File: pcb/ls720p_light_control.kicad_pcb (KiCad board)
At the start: 2 copper layers, 40 x 20 mm, 20 parts, among them J1 PWR, J2 AVRISP MK2, J3 LED_CONN, Q1 G35N02K, U1 ATTINY5, U2 SLHT50H

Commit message: added ALT parts for LDO, MOSFET, MCU
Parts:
- added SW1: PWR_SWITCH, Connector_PinHeader_2.54mm:PinHeader_1x02_P2.54mm_Vertical, F.Cu at (210.0, 106.7)
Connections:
- J1 pad 2: +12V -> Net-(J1-Pin_2)
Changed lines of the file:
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@@
 			(layers "*.Cu" "*.Mask")
 			(remove_unused_layers no)
-			(net "+12V")
+			(net "Net-(J1-Pin_2)")
 			(pinfunction "Pin_2_2")
 			(pintype "passive")
@@
 			(pintype "passive")
 		)
+		(embedded_fonts no)
+		(model "${KICAD10_3DMODEL_DIR}/Connector_PinHeader_2.54mm.3dshapes/PinHeader_1x02_P2.54mm_Vertical.step"
+			(offset
+				(xyz 0 0 0)
+			)
+			(scale
+				(xyz 1 1 1)
+			)
+			(rotate
+				(xyz 0 0 0)
+			)
+		)
+	)
+	(footprint "Connector_PinHeader_2.54mm:PinHeader_1x02_P2.54mm_Vertical"
+		(layer "F.Cu")
+		(at 209.975 106.7 -90)
+		(descr "Through hole straight pin header, 1x02, 2.54mm pitch, single row")
+		(tags "Through hole pin header THT 1x02 2.54mm single row")
+		(property "Reference" "SW1"
+			(at 0 -2.725 270)
+			(layer "F.SilkS")
+			(effects
+				(font
+					(size 1 1)
+					(thickness 0.15)
+				)
+			)
+		)
+		(property "Value" "PWR_SWITCH"
+			(at 0 4.919999 90)
+			(layer "F.Fab")
+			(effects
+				(font
+					(size 1 1)
+					(thickness 0.15)
+				)
+			)
+		)
+		(property "Datasheet" ""
+			(at 0 0 90)
+			(layer "F.Fab")
+			(hide yes)
+			(effects
+				(font
+					(size 1.27 1.27)
+				)
+			)
+		)
+		(property "Description" "Single Pole Single Throw (SPST) switch"
+			(at 0 0 90)
+			(layer "F.Fab")
+			(hide yes)
+			(effects
+				(font
+					(size 1.27 1.27)
+				)
+			)
+		)
+		(property "KiLib_Generator" "connector/pin_header_socket"
+			(at 0 0 90)
+			(layer "F.SilkS")
+			(hide yes)
+			(effects
+				(font
+					(size 1 1)
+					(thickness 0.15)
+				)
+			)
+		)
+		(sheetname "/")
+		(sheetfile "ls720p_light_control.kicad_sch")
+		(units
+			(unit
+				(name "A")
+				(pins "1" "2")
+			)
+		)
+		(attr through_hole)
+		(duplicate_pad_numbers_are_jumpers no)
+		(fp_line
+			(start -1.38 3.92)
+			(end 1.38 3.92)
+			(stroke
+				(width 0.12)
+				(type solid)
+			)
+			(layer "F.SilkS")
+		)
+		(fp_line
+			(start -1.38 1.27)
+			(end -1.38 3.92)
+			(stroke
+				(width 0.12)
+				(type solid)
+			)
+			(layer "F.SilkS")
+		)
+		(fp_line
+			(start -1.38 1.27)
+			(end 1.38 1.27)
+			(stroke
+				(width 0.12)
+				(type solid)
+			)
+			(layer "F.SilkS")
+		)
+		(fp_line
+			(start 1.38 1.27)
+			(end 1.38 3.92)
+			(stroke
+				(width 0.12)
+				(type solid)
+			)
+			(layer "F.SilkS")
+		)
+		(fp_line
+			(start -1.379999 0)
+			(end -1.38 -1.38)
+			(stroke
+				(width 0.12)
+				(type solid)
+			)
+			(layer "F.SilkS")
+		)
+		(fp_line
+			(start -1.38 -1.38)
+			(end 0 -1.379999)
+			(stroke
+				(width 0.12)
+				(type solid)
+			)
+			(layer "F.SilkS")
+		)
+		(fp_poly
+			(pts
+				(xy -1.77 -1.77) (xy 1.77 -1.77) (xy 1.77 4.32) (xy -1.77 4.32)
+			)
+			(stroke
+				(width 0.05)
+				(type solid)
+			)
+			(fill no)
+			(layer "F.CrtYd")
+		)
+		(fp_line
+			(start -1.27 3.81)
+			(end -1.27 -0.635)
+			(stroke
+				(width 0.1)
+				(type solid)
+			)
+			(layer "F.Fab")
+		)
+		(fp_line
+			(start 1.27 3.81)
+			(end -1.27 3.81)
+			(stroke
+				(width 0.1)
+				(type solid)
+			)
+			(layer "F.Fab")
+		)
+		(fp_line
+			(start -1.27 -0.635)
+			(end -0.635 -1.27)
+			(stroke
+				(width 0.1)
+				(type solid)
+			)
+			(layer "F.Fab")
+		)
+		(fp_line
+			(start -0.635 -1.27)
+			(end 1.27 -1.27)
+			(stroke
+				(width 0.1)
+				(type solid)
+			)
+			(layer "F.Fab")
+		)
+		(fp_line
+			(start 1.27 -1.27)
+			(end 1.27 3.81)
+			(stroke
+				(width 0.1)
+				(type solid)
+			)
+			(layer "F.Fab")
+		)
+		(fp_text user "${REFERENCE}"
+			(at 0 1.270001 0)
+			(layer "F.Fab")
+			(effects
+				(font
+					(size 1 1)
+					(thickness 0.15)
+				)
+			)
+		)
+		(pad "1" thru_hole rect
+			(at 0 0 270)
+			(size 1.7 1.7)
+			(drill 1)
+			(layers "*.Cu" "*.Mask")
+			(remove_unused_layers no)
+			(net "Net-(J1-Pin_2)")
+			(pinfunction "A_1")
+			(pintype "passive")
+		)
+		(pad "2" thru_hole circle
+			(at 0 2.54 270)
+			(size 1.7 1.7)
+			(drill 1)
+			(layers "*.Cu" "*.Mask")
+			(remove_unused_layers no)
+			(net "+12V")
+			(pinfunction "B_2")
+			(pintype "passive")
+		)

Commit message: done placing components
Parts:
- added REF**: MountingHole_3.2mm_M3, MountingHole:MountingHole_3.2mm_M3, B.Cu at (218.0, 106.0)
- added RV1: 10k, Connector_PinHeader_2.54mm:PinHeader_1x03_P2.54mm_Vertical, B.Cu at (217.8, 92.5)
- J1, J3, SW1: moved to B.Cu
- Q1: value G35N02K -> G35N02K/IRLR7843TR
- U1: value ATTINY5 -> ATTINY5/ATTINY10
- U2: value SLHT50H -> SLHT50H/HT7550
- moved D1 101.2 mm to (-24.9, 150.1)
- moved R6 101.2 mm to (-25.4, 154.7)
- moved C1 7.23 mm to (222.6, 96.4), turned to -90 degrees
- moved SW1 6.36 mm to (203.6, 107.0)
- moved R3 5.57 mm to (219.7, 95.4), turned to 180 degrees
- moved C2 3.81 mm to (218.4, 101.1)
- moved U1 3.71 mm to (218.4, 98.2)
- moved J1 2.50 mm to (203.2, 99.7), turned to 180 degrees
- moved U2 1.70 mm to (210.9, 103.0)
- moved R2 1.54 mm to (203.8, 95.3), turned to 90 degrees
- moved C3 1.49 mm to (206.4, 102.8)
- moved R1 1.30 mm to (201.8, 95.3), turned to -90 degrees
- moved C6 1.12 mm to (210.6, 99.6)
- moved C7 1.10 mm to (236.4, 105.0), turned to 0 degrees
- moved C5 0.92 mm to (236.4, 102.6), turned to 0 degrees
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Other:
- board text added: "+ -"
- board text added: "- ADJ +"
- board text added: "AJ747/ ls720p-light-control Rev 1 10.05.26"
- board text added: "LED"
- board text added: "VIN 5-12V"

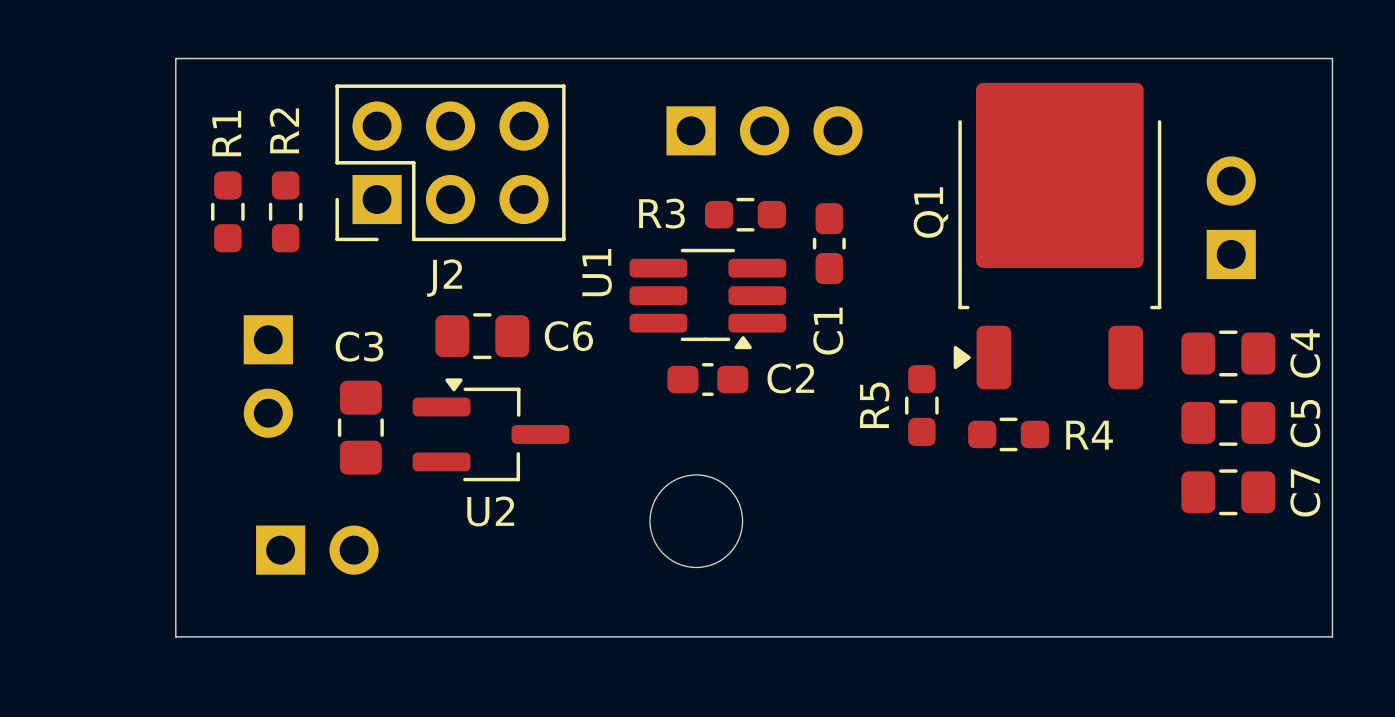
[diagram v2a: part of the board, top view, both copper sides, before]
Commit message: pcb -> updated placing
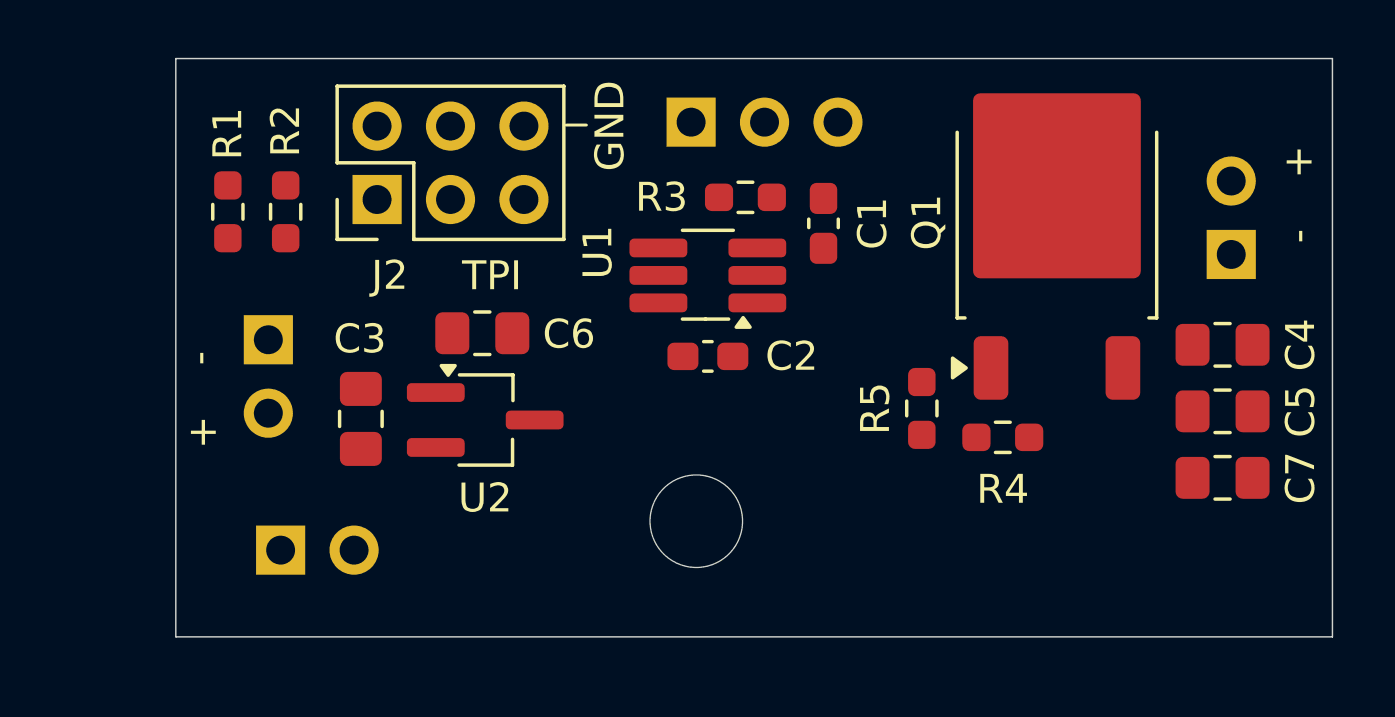
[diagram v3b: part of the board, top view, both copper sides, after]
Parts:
- moved C2 0.80 mm to (218.4, 100.3)
- moved C1 0.73 mm to (222.4, 95.7)
- moved U1 0.70 mm to (218.4, 97.5)
- moved R3 0.60 mm to (219.7, 94.8)
- moved C7 0.54 mm to (236.2, 104.5), turned to 180 degrees
- moved U2 0.54 mm to (210.7, 102.5)
- moved C5 0.45 mm to (236.2, 102.2), turned to 180 degrees
- moved Q1 0.37 mm to (230.5, 95.7)
- moved C4 0.36 mm to (236.2, 99.9), turned to 180 degrees
- moved C3 0.30 mm to (206.4, 102.5)
- moved RV1 0.30 mm to (217.8, 92.2)
- moved R4 0.22 mm to (228.6, 103.1)
- moved C6 0.10 mm to (210.6, 99.5)
- moved R5 0.10 mm to (225.8, 102.1)
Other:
- board text added: "GND"
- board text added: "TPI"

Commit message: pcb -> finished layout, need to add stitching vias
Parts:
- removed D1: RED, Diode_SMD:D_0603_1608Metric_Pad1.05x0.95mm_HandSolder
- removed R6: 1k, Resistor_SMD:R_0603_1608Metric_Pad0.98x0.95mm_HandSolder
- moved R1 0.60 mm to (202.4, 95.3), turned to 90 degrees
- moved R2 0.30 mm to (204.1, 95.3)
- renumbered C4 to C3, C3 to C4, C7 to C6, C6 to C7
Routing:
- net /LED_CONTROL_PWM: track 0.00 -> 28.8 mm, vias 0 -> 1
- net +5V: track 0.00 -> 23.9 mm
- net /BRIGHTNESS_ADJ_MAX: track 0.00 -> 15.3 mm
- net /TPICLK: track 0.00 -> 12.7 mm, vias 0 -> 2
- net +12V: track 0.00 -> 9.60 mm
- net /~{RESET}: track 0.00 -> 6.58 mm, vias 0 -> 1
- net GND: track 0.00 -> 5.28 mm, vias 0 -> 7
- net Net-(J1-Pin_2): track 0.00 -> 4.91 mm
- net /BRIGHTNESS_ADJ: track 0.00 -> 4.51 mm
- net Net-(Q1-G): track 0.00 -> 2.59 mm
- added copper zone on F.Cu, net +12V
- added copper zone on F.Cu, net +5V
- added copper zone on B.Cu, net GND
- added copper zone on F.Cu, net GND
- added copper zone on F.Cu, net Net-(J3-Pin_2)

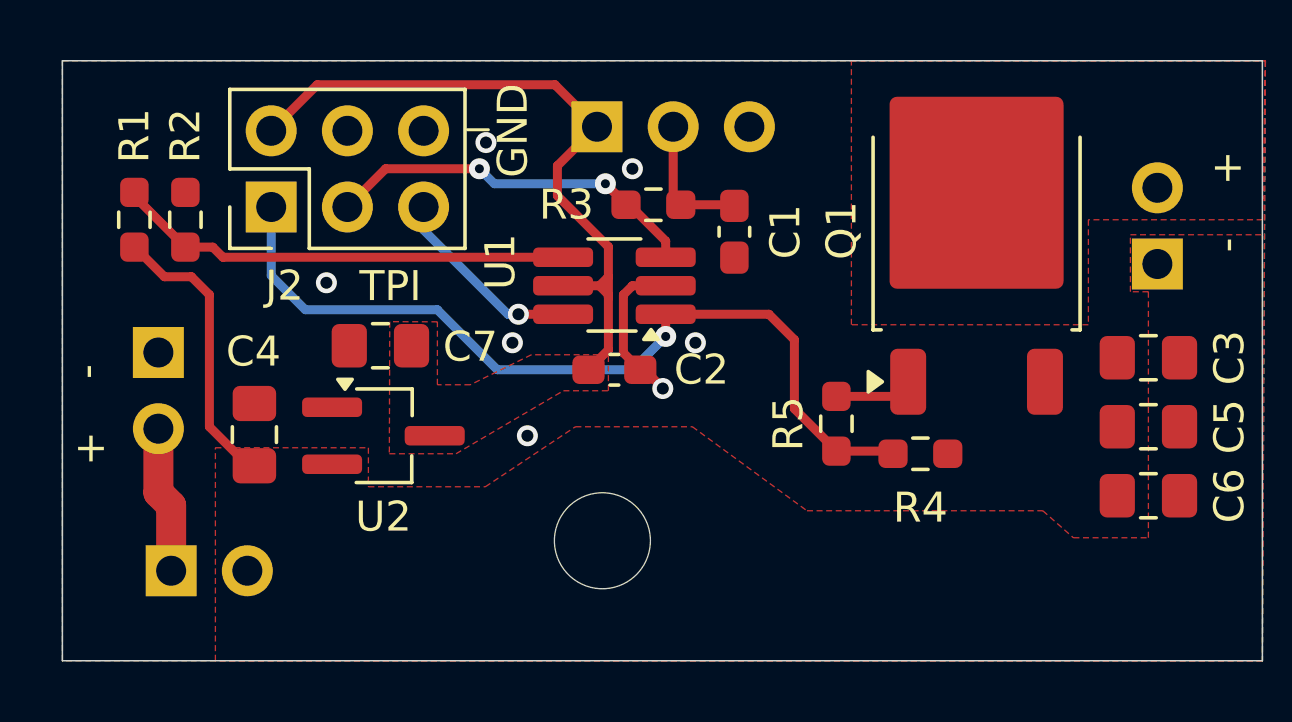
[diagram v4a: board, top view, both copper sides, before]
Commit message: pcb -> layout completed
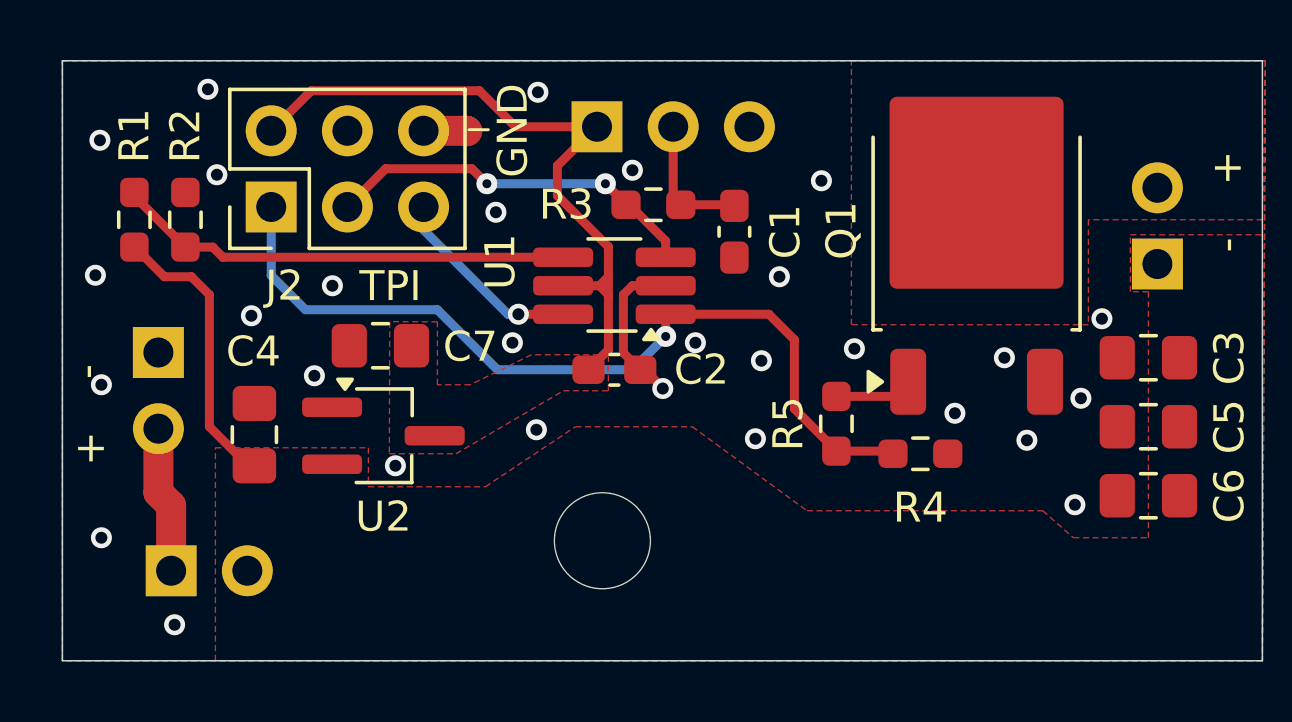
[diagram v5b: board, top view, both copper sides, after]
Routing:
- net GND: track 5.28 -> 6.75 mm, vias 7 -> 29

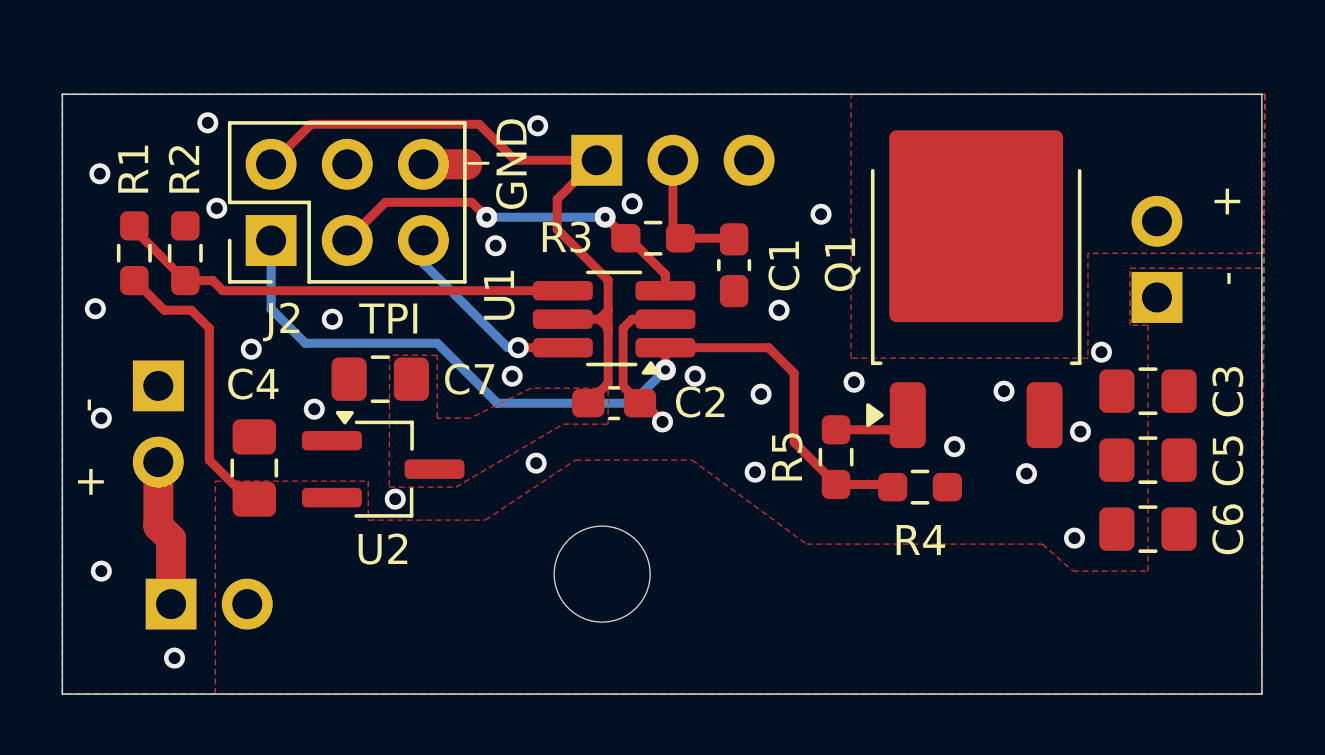
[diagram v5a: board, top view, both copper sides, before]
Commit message: removed +12v rail, everything is now +5v
using +12v didn't acheive better brightness when using pwm, so keeping +5v
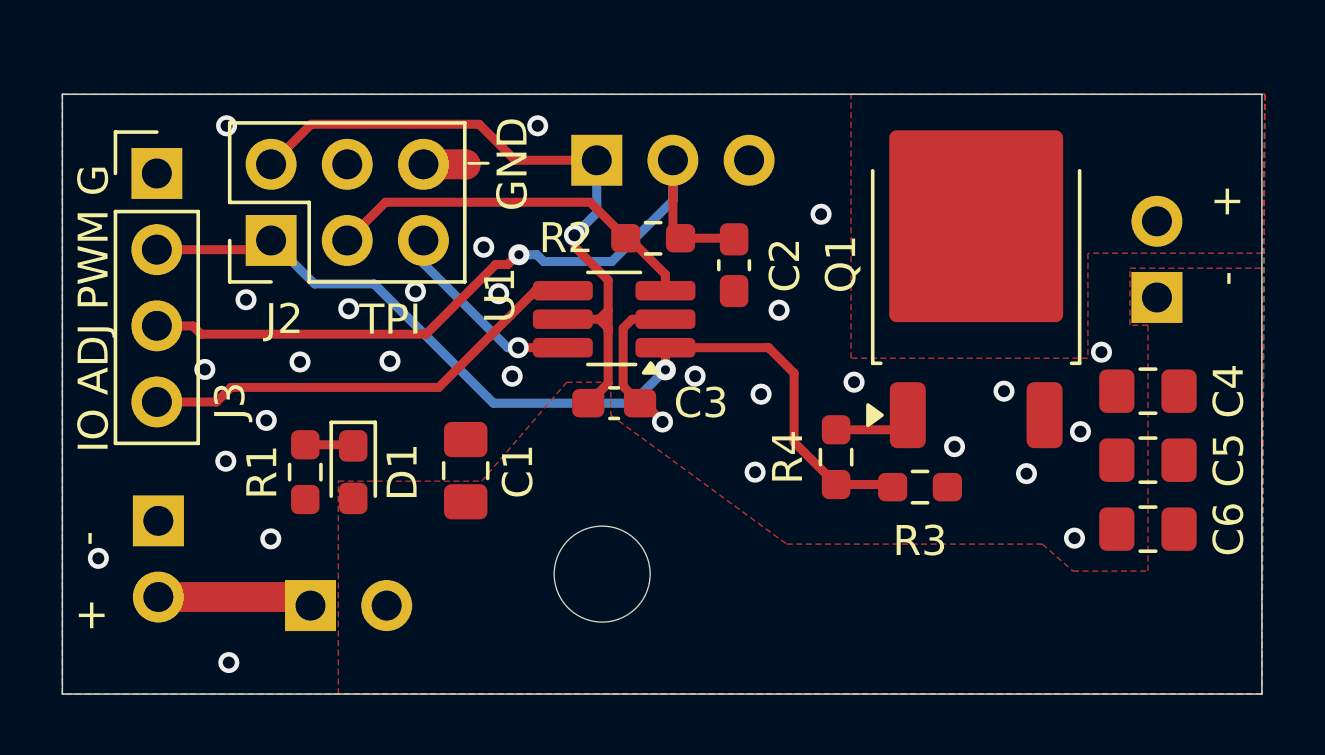
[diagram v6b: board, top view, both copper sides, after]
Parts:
- removed the C4 at (206.4, 102.5)
- removed C7: 10u, Capacitor_SMD:C_0805_2012Metric_Pad1.18x1.45mm_HandSolder
- removed the R2 at (204.1, 95.3)
- removed U2: SLHT50H/HT7550, Package_TO_SOT_SMD:TSOT-23_HandSoldering
- added C1: 10u, Capacitor_SMD:C_0805_2012Metric_Pad1.18x1.45mm_HandSolder, F.Cu at (213.4, 102.5)
- added D1: RED, LED_SMD:LED_0603_1608Metric_Pad1.05x0.95mm_HandSolder, F.Cu at (209.7, 102.6)
- added J3: Conn_01x04, Connector_PinHeader_2.54mm:PinHeader_1x04_P2.54mm_Vertical, F.Cu at (203.2, 92.6)
- R1: value 15k -> 1k
- moved R1 9.26 mm to (208.1, 102.6)
- moved SW1 4.65 mm to (208.3, 107.0)
- moved J1 4.50 mm to (203.2, 104.2)
- renumbered C1 to C2, C2 to C3, C3 to C4, J3 to J4, R3 to R2, R4 to R3, R5 to R4
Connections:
- C4 pad 1: +12V -> +5V
- C5 pad 1: +12V -> +5V
- C6 pad 1: +12V -> +5V
- J4 pad 1: +12V -> +5V
- R1 pad 1: +12V -> GND
- R1 pad 2: /BRIGHTNESS_ADJ_MAX -> Net-(D1-K)
- SW1 pad 2: +12V -> +5V
- U1 pad 4: /BRIGHTNESS_ADJ_MAX -> /DBG_IO
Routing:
- net /BRIGHTNESS_ADJ: track 4.51 -> 25.2 mm, vias 0 -> 1
- net /BRIGHTNESS_ADJ_MAX: track 15.3 -> 0.00 mm
- net /DBG_IO: track 0.00 -> 15.1 mm
- net +12V: track 9.60 -> 0.00 mm
- net /LED_CONTROL_PWM: track 28.8 -> 31.4 mm
- net Net-(D1-K): track 0.00 -> 1.62 mm
- net +5V: track 23.7 -> 23.2 mm, vias 0 -> 1
- net /TPICLK: vias 2 -> 0
- removed copper zone on F.Cu, net +12V
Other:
- board text added: "+5V"
- board text added: "IO ADJ PWM G"
- board text removed: "VIN 5-12V"

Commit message: updated pictures and pcb
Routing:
- net GND: vias 29 -> 30
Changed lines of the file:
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@@
+	)
+	(via
+		(at 215.5444 94.3356)
+		(size 0.7)
+		(drill 0.4)
+		(layers "F.Cu" "B.Cu")
+		(net "GND")
 	)
 	(via
